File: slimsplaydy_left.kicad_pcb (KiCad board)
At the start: 2 copper layers, 115.1 x 87.3 mm, 24 parts

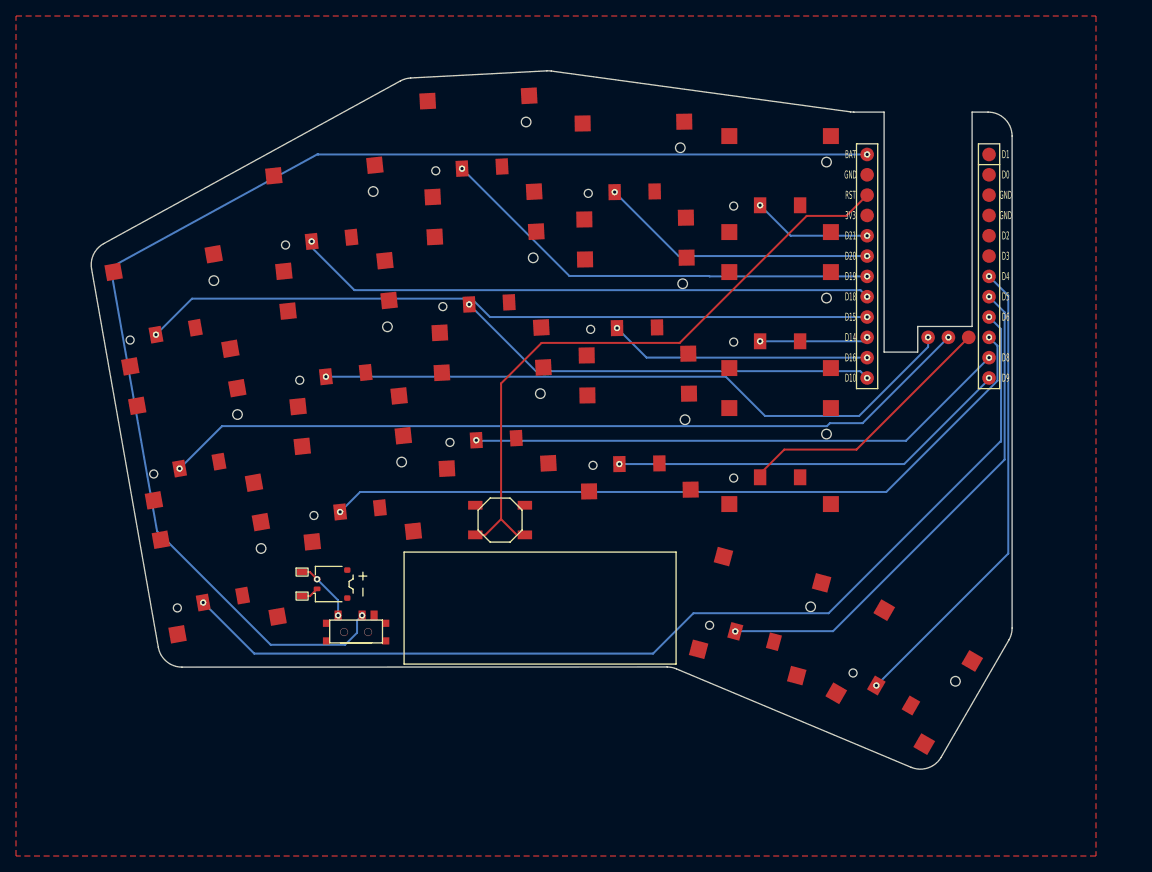
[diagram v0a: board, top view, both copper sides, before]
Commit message: Create first draft design and routing for both sides.
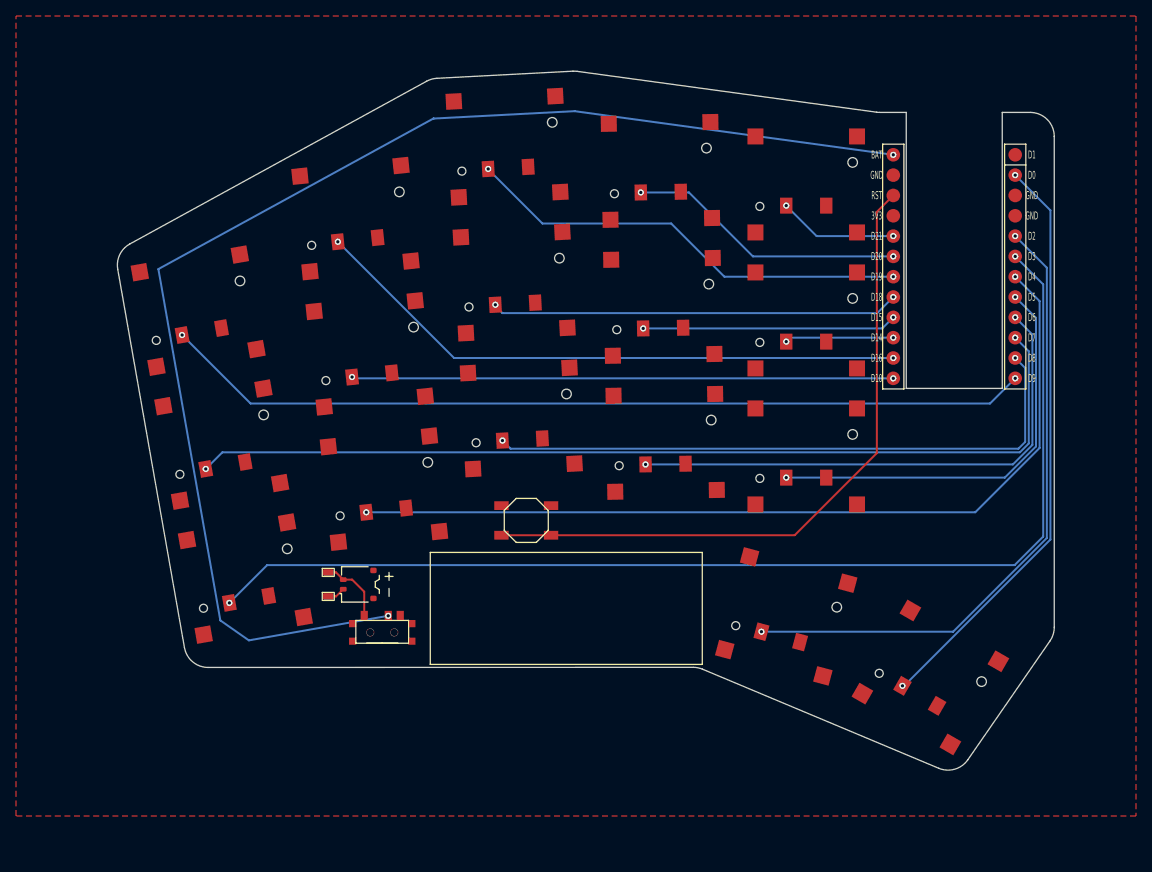
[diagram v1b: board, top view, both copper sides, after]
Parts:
- moved S6 3.27 mm to (122.4, 100.3)
- moved S10 3.27 mm to (161.1, 128.4)
- moved B1 3.27 mm to (143.8, 138.1), turned to 0 degrees
- moved S1 3.27 mm to (108.7, 145.3)
- moved T1 3.27 mm to (125.8, 152.1)
- moved S16 3.27 mm to (176.3, 150.1)
- moved S5 3.27 mm to (124.2, 117.2)
- moved S14 3.27 mm to (178.8, 113.1), turned to 0 degrees
- moved S17 3.27 mm to (194.3, 157.7)
- moved S8 3.27 mm to (142.3, 108.3)
- moved S7 3.27 mm to (143.2, 125.3)
- moved XX3 3.27 mm to (131.8, 142.1), turned to 0 degrees
- moved S4 3.27 mm to (126.0, 134.1)
- moved CONN1 3.27 mm to (122.8, 146.1)
- moved XX1 3.27 mm to (118.3, 144.1), turned to 0 degrees
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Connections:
- MCU1 pad 10: hand_ring_bottom -> hand_pinky_home
- MCU1 pad 12: hand_index_bottom -> hand_pinky_top
- MCU1 pad 13: hand_middle_home -> hand_ring_home
- MCU1 pad 14: hand_index_home -> hand_ring_top
- MCU1 pad 16: hand_pinky_top -> hand_index_home
- MCU1 pad 17: hand_ring_top -> hand_middle_home
- MCU1 pad 2: D0 -> thumb_far_fan
- MCU1 pad 5: D2 -> thumb_near_fan
- MCU1 pad 6: D3 -> hand_pinky_bottom
- MCU1 pad 7: thumb_far_fan -> hand_ring_bottom
- MCU1 pad 8: thumb_near_fan -> hand_inner_bottom
- MCU1 pad 9: hand_pinky_bottom -> hand_index_bottom
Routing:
- net hand_inner_bottom: track 33.6 -> 52.6 mm, vias 0 -> 2
- net hand_pinky_top: track 91.7 -> 109.0 mm
- net thumb_near_fan: track 63.7 -> 79.9 mm
- net hand_index_bottom: track 50.8 -> 66.2 mm
- net hand_ring_bottom: track 94.8 -> 110.2 mm
- net hand_pinky_home: track 102.9 -> 118.1 mm
- net thumb_far_fan: track 59.0 -> 73.4 mm
- net hand_ring_home: track 82.1 -> 67.7 mm
- net hand_pinky_bottom: track 129.5 -> 141.6 mm
- net hand_middle_bottom: track 68.4 -> 77.1 mm
- net RST: track 80.3 -> 84.2 mm
- net hand_ring_top: track 72.7 -> 75.4 mm
- net hand_middle_home: track 53.6 -> 51.1 mm
- net BAT: track 165.6 -> 163.7 mm
- net hand_index_home: track 32.8 -> 31.8 mm
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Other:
- board size 115.1 x 87.3 mm -> 117.1 x 87.4 mm

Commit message: Finish layout, schematic, routing.
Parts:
- removed B1: , E73:SW_TACT_ALPS_SKQGABE010
- removed T1: , E73:SPDT_C128955
- removed XX1, XX2: , Pad_Single_BAT-
- removed XX3: , Battery_301230
- added MAG1: , magsafe, B.Cu at (45.0, -32.5)
- added MH1: , ceoloide:mounting_hole_npth, F.Cu at (91.9, 28.8)
- added MH10: , ceoloide:mounting_hole_npth, F.Cu at (29.0, -8.95)
- added MH11: , ceoloide:mounting_hole_npth, F.Cu at (8.05, 11.5)
- added MH12: , ceoloide:mounting_hole_npth, F.Cu at (-7.92, 11.9)
- added MH13: , ceoloide:mounting_hole_npth, F.Cu at (-15.9, -42.7)
- added MH14: , ceoloide:mounting_hole_npth, F.Cu at (2.96, -51.8)
- added MH15: , ceoloide:mounting_hole_npth, F.Cu at (61.0, -60.5)
- added MH2: , ceoloide:mounting_hole_npth, F.Cu at (-13.0, -15.3)
- added MH3: , ceoloide:mounting_hole_npth, F.Cu at (35.0, -64.8)
- added MH4: , ceoloide:mounting_hole_npth, F.Cu at (77.0, -57.8)
- added MH5: , ceoloide:mounting_hole_npth, F.Cu at (101.5, -55.5)
- added MH6: , ceoloide:mounting_hole_npth, F.Cu at (90.0, -21.5)
- added MH7: , ceoloide:mounting_hole_npth, F.Cu at (82.5, 0.55)
- added MH8: , ceoloide:mounting_hole_npth, F.Cu at (101.0, 8.55)
- added MH9: , ceoloide:mounting_hole_npth, F.Cu at (60.0, 15.1)
- added PWR1: Power SW, ceoloide:power_switch_smd_side, F.Cu at (101.8, -1.45)
- added RST1: Reset SW, ceoloide:reset_switch_smd_side, F.Cu at (101.0, -12.5)
- CONN1: value (none) -> Battery Connector; footprint ceoloide:battery_connector_molex_pico_ezmate_1x02 -> Molex_Pico_EZMate_Plus_1x02
- MCU1: value (none) -> nice_nano
- S1, S10, S11, S12, S13, S14, S15, S16, S17, S2, S3, S4, S5, S6, S7, S8, S9: value (none) -> PG1316S; footprint CPG1316S01D02_mikeholscher -> PG1316S
- moved S4 183.5 mm to (17.0, -13.5), turned to 3 degrees
- moved S5 183.0 mm to (16.1, -30.5), turned to 3 degrees
- moved S6 182.6 mm to (15.2, -47.4), turned to 3 degrees
- moved MCU1 181.6 mm to (90.0, -41.5)
- moved S7 181.5 mm to (35.0, -20.5), turned to 0 degrees
- moved S1 181.5 mm to (0.00, 0.00), turned to 8 degrees
- moved S2 181.2 mm to (-2.37, -16.8), turned to 8 degrees
- moved S8 181.0 mm to (35.0, -37.5), turned to 0 degrees
- moved S3 180.9 mm to (-4.73, -33.7), turned to 8 degrees
- moved S9 180.5 mm to (35.0, -54.5), turned to 0 degrees
- moved S10 179.9 mm to (53.0, -15.5), turned to 0 degrees
- moved S11 179.7 mm to (53.0, -32.5), turned to 0 degrees
- moved S12 179.6 mm to (53.0, -49.5), turned to 0 degrees
- moved S13 179.4 mm to (71.0, -13.5)
- moved S15 179.4 mm to (71.0, -47.5)
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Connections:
- net hand_index_top renamed finger_index_top
- net hand_inner_top renamed finger_inner_top
- net hand_middle_top renamed finger_middle_top
- MCU1 pad 1: D1 -> finger_inner_home
- MCU1 pad 10: hand_pinky_home -> finger_pinky_top
- MCU1 pad 11: hand_middle_bottom -> thumb_tucky_fan
- MCU1 pad 12: hand_pinky_top -> thumb_reachy_fan
- MCU1 pad 13: hand_ring_home -> finger_index_home
- MCU1 pad 14: hand_ring_top -> finger_middle_home
- MCU1 pad 15: hand_inner_home -> finger_ring_home
- MCU1 pad 16: hand_index_home -> finger_pinky_home
- MCU1 pad 17: hand_middle_home -> finger_ring_top
- MCU1 pad 2: thumb_far_fan -> unconnected-(MCU1-P0.08-Pad2)
- MCU1 pad 21: 3V3 -> unconnected-(MCU1-3V3-Pad21)
- MCU1 pad 24: BAT -> RAW
- MCU1 pad 5: thumb_near_fan -> finger_pinky_bottom
- MCU1 pad 6: hand_pinky_bottom -> finger_ring_bottom
- MCU1 pad 7: hand_ring_bottom -> finger_middle_bottom
- MCU1 pad 8: hand_inner_bottom -> finger_index_bottom
- MCU1 pad 9: hand_index_bottom -> finger_inner_bottom
- S1 pad 1: hand_pinky_bottom -> finger_pinky_bottom
- S1 pad 3: (no net) -> GND
- S10 pad 1: hand_index_bottom -> finger_index_bottom
- S10 pad 3: (no net) -> GND
- S11 pad 1: hand_index_home -> finger_index_home
- S11 pad 3: (no net) -> GND
- S12 pad 3: (no net) -> GND
- S13 pad 1: hand_inner_bottom -> finger_inner_bottom
- S13 pad 3: (no net) -> GND
- S14 pad 1: hand_inner_home -> finger_inner_home
- S14 pad 3: (no net) -> GND
- S15 pad 3: (no net) -> GND
- S16 pad 1: thumb_near_fan -> thumb_tucky_fan
- S16 pad 3: (no net) -> GND
- S17 pad 1: thumb_far_fan -> thumb_reachy_fan
- S17 pad 3: (no net) -> GND
- S2 pad 1: hand_pinky_home -> finger_pinky_home
- S2 pad 3: (no net) -> GND
- S3 pad 1: hand_pinky_top -> finger_pinky_top
- S3 pad 3: (no net) -> GND
- S4 pad 1: hand_ring_bottom -> finger_ring_bottom
- S4 pad 3: (no net) -> GND
- S5 pad 1: hand_ring_home -> finger_ring_home
- S5 pad 3: (no net) -> GND
- S6 pad 1: hand_ring_top -> finger_ring_top
- S6 pad 3: (no net) -> GND
- S7 pad 1: hand_middle_bottom -> finger_middle_bottom
- S7 pad 3: (no net) -> GND
- S8 pad 1: hand_middle_home -> finger_middle_home
- S8 pad 3: (no net) -> GND
- S9 pad 3: (no net) -> GND
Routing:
- net BAT: track 163.7 -> 0.00 mm, vias 2 -> 0
- net finger_pinky_bottom: track 0.00 -> 142.8 mm
- net hand_pinky_bottom: track 141.6 -> 0.00 mm, vias 2 -> 0
- net finger_pinky_top: track 0.00 -> 129.8 mm
- net finger_pinky_home: track 0.00 -> 125.3 mm
- net finger_middle_bottom: track 0.00 -> 122.0 mm
- net finger_ring_bottom: track 0.00 -> 120.4 mm
- net hand_pinky_home: track 118.1 -> 0.00 mm, vias 2 -> 0
- net hand_ring_bottom: track 110.2 -> 0.00 mm, vias 2 -> 0
- net hand_pinky_top: track 109.0 -> 0.00 mm, vias 2 -> 0
- net thumb_near_fan: track 79.9 -> 0.00 mm, vias 2 -> 0
- net finger_ring_top: track 0.00 -> 78.7 mm
- net finger_index_bottom: track 0.00 -> 78.6 mm
- net hand_middle_bottom: track 77.1 -> 0.00 mm, vias 2 -> 0
- net finger_ring_home: track 0.00 -> 76.1 mm
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- added copper zone on B.Cu, net GND
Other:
- board size 117.1 x 87.4 mm -> 122.6 x 97.5 mm

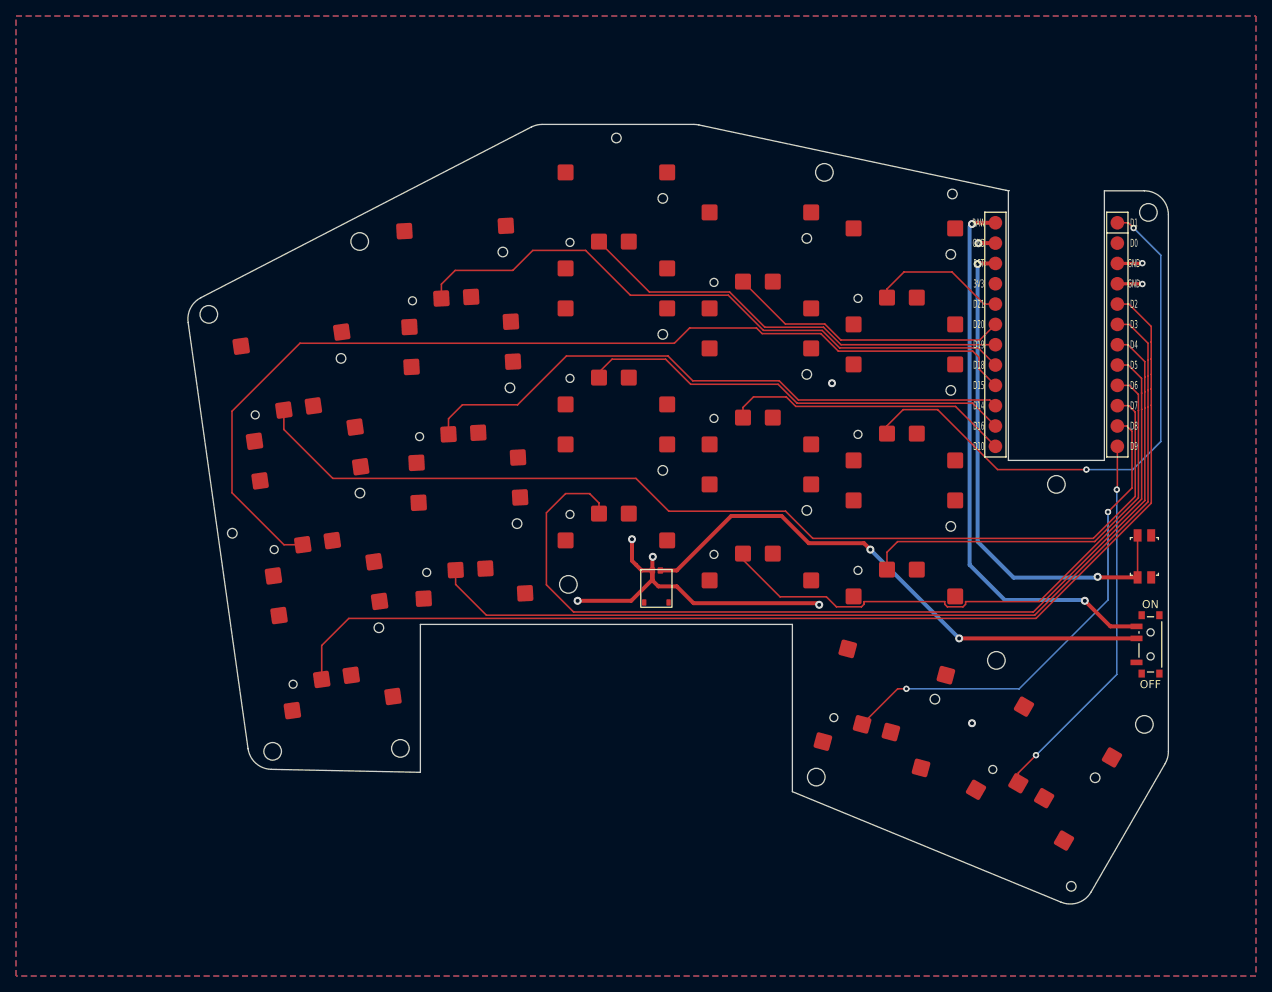
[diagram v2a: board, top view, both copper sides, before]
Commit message: Fix MCU slots. Fillet outline. Reroute both sides. Re-re-reroute both sides.
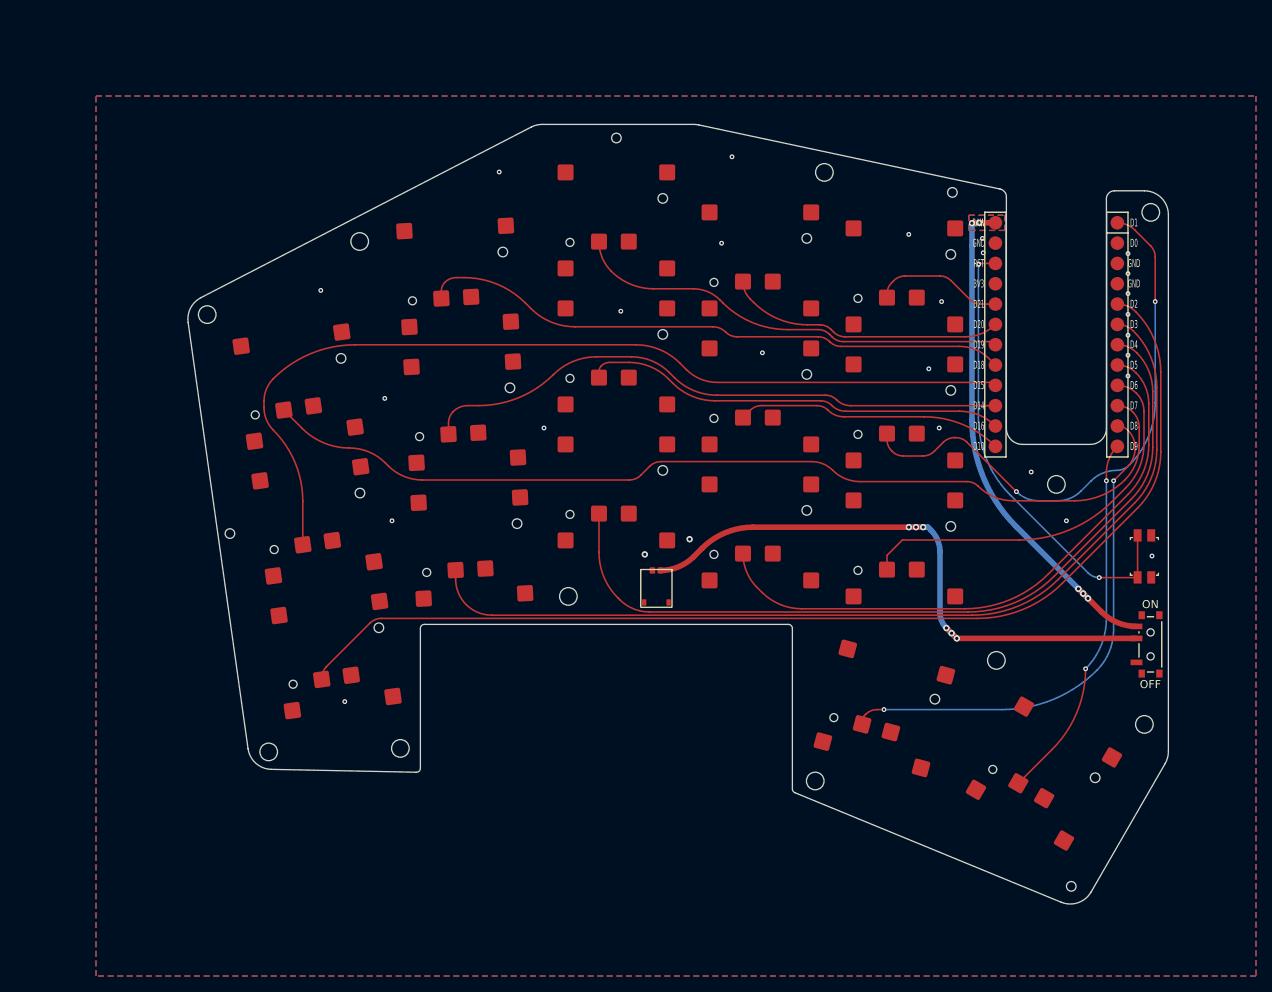
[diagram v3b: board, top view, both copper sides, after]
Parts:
- moved MH10 1.50 mm to (29.0, -7.45)
- moved MH9 0.50 mm to (59.9, 15.6)
- moved MH12 0.50 mm to (-8.41, 12.0)
- moved MH5 0.30 mm to (101.8, -55.5)
- moved MH2 0.30 mm to (-13.3, -15.3)
- moved MH13 0.20 mm to (-16.1, -42.7)
- moved MH4 0.20 mm to (77.0, -58.0)
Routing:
- net GND: track 50.8 -> 0.00 mm, vias 9 -> 28
- net finger_middle_bottom: track 122.0 -> 103.0 mm
- net finger_pinky_home: track 125.3 -> 115.0 mm
- net finger_pinky_top: track 129.8 -> 121.7 mm
- net BAT_P: track 68.7 -> 76.2 mm, vias 2 -> 6
- net RST: track 64.1 -> 57.4 mm
- net RAW: track 69.8 -> 63.9 mm, vias 2 -> 5
- net finger_ring_top: track 78.7 -> 74.1 mm
- net finger_pinky_bottom: track 142.8 -> 139.1 mm
- net thumb_tucky_fan: track 61.6 -> 65.1 mm
- net finger_inner_bottom: track 52.4 -> 49.6 mm
- net finger_index_bottom: track 78.6 -> 75.8 mm
- net finger_index_home: track 35.9 -> 33.4 mm
- net finger_ring_home: track 76.1 -> 74.1 mm
- net finger_ring_bottom: track 120.4 -> 118.7 mm
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- added copper zone on B.Cu, net RAW
- added copper zone on F.Cu, net RAW
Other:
- outline, holes or cut-outs redrawn

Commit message: Add production files.
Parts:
- moved MCU1 0.20 mm to (90.0, -41.7)
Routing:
- net thumb_tucky_fan: track 65.1 -> 61.3 mm
- net finger_pinky_top: track 121.7 -> 125.2 mm
- net RAW: track 63.9 -> 66.5 mm, vias 5 -> 7
- net finger_pinky_home: track 115.0 -> 113.0 mm
- net RST: track 57.4 -> 59.1 mm
- net finger_middle_home: track 53.0 -> 54.6 mm
- net finger_index_home: track 33.4 -> 34.4 mm
- net BAT_P: track 76.2 -> 75.1 mm
- net finger_index_bottom: track 75.8 -> 76.9 mm
- net finger_ring_home: track 74.1 -> 73.1 mm
- net finger_middle_bottom: track 103.0 -> 102.5 mm
- net GND: vias 28 -> 33
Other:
- outline, holes or cut-outs redrawn
